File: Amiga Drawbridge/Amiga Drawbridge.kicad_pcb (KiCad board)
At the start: 2 copper layers, 90 x 94 mm, 19 parts, among them J1 FDC, J2 PWR_EXT1, J3 PWR_DRV, J4 PWR_EXT2, M1 Mounting, M2 Mounting, M3 Mounting, M4 Mounting

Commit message: Changed power pin order
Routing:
- net Net-(D1-Pad2): track 126.8 -> 128.6 mm
- net Net-(J3-Pad4): track 15.0 -> 16.6 mm
- net GND: track 0.00 -> 1.27 mm

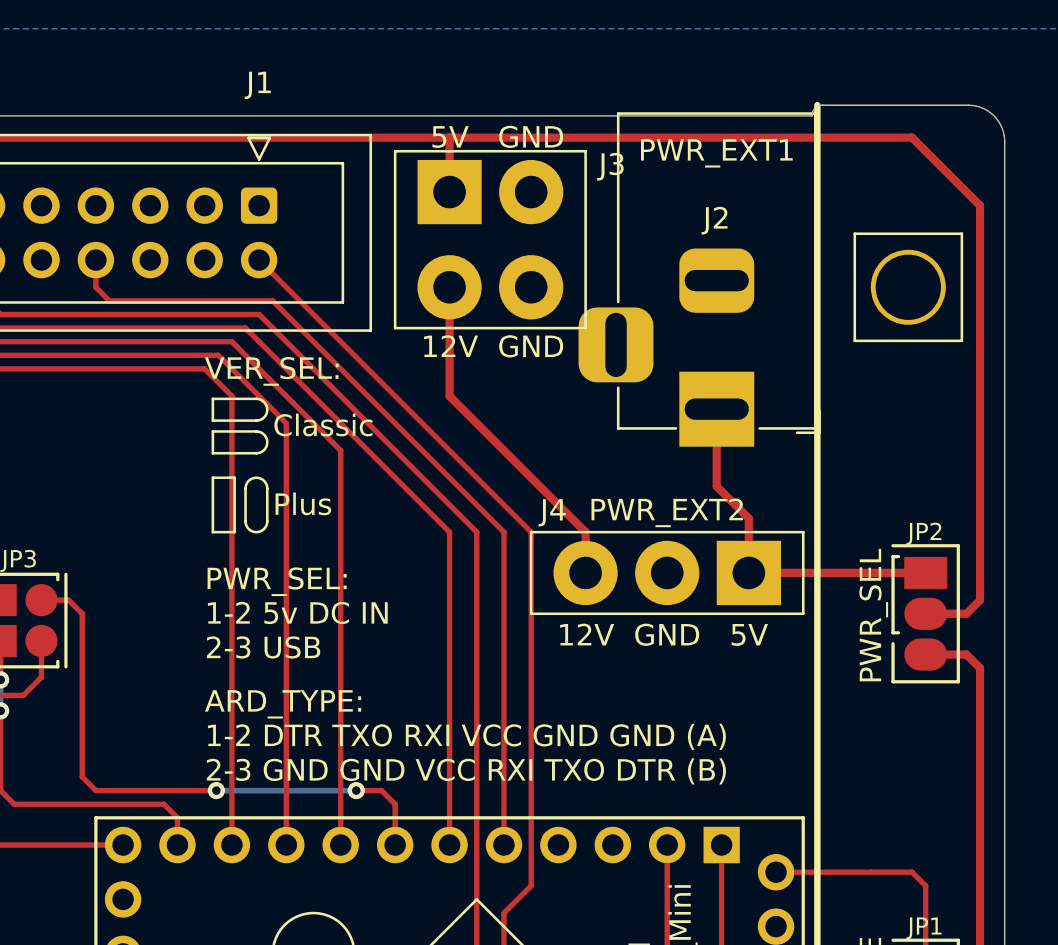
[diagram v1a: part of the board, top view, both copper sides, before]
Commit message: PWR_EXT2 renamed PWR_IN2, now 4 pin to match greaseweazle
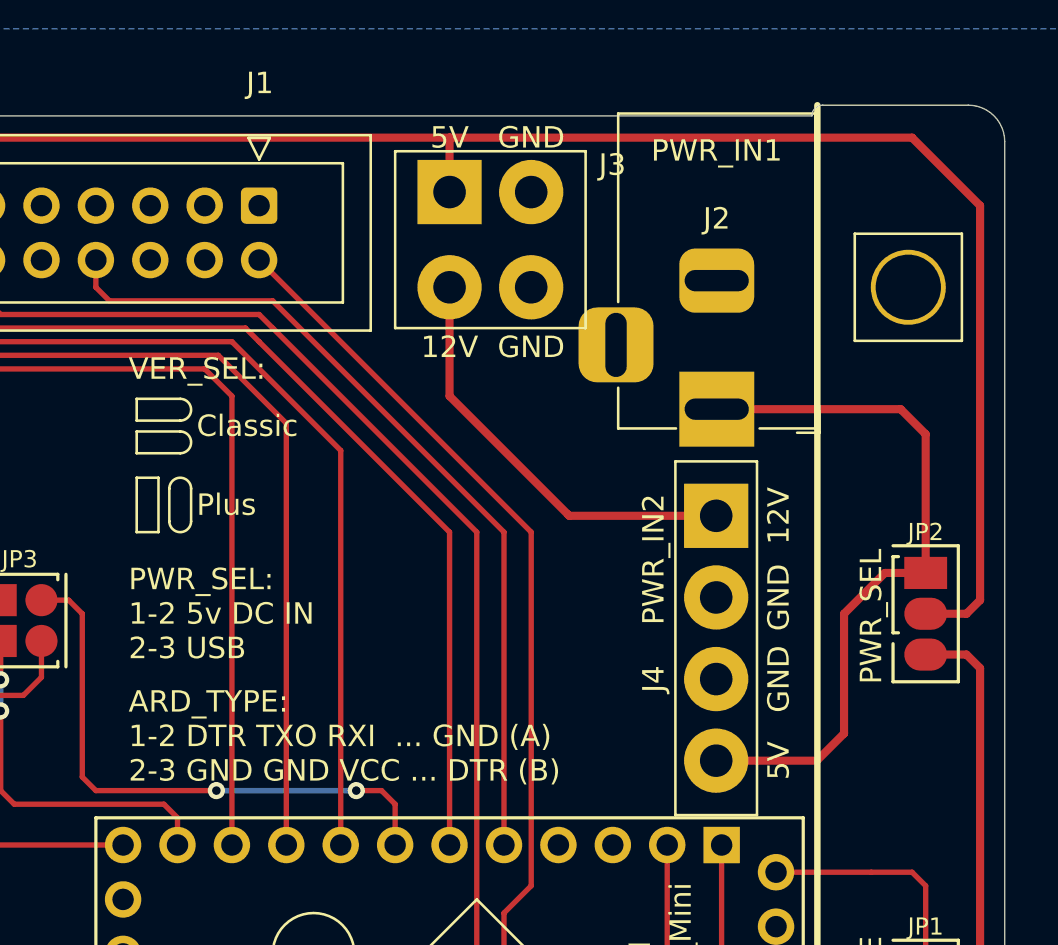
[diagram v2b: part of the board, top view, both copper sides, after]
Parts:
- J2: value PWR_EXT1 -> PWR_IN1
- J4: value PWR_EXT2 -> PWR_IN2; footprint pwr_drv:PWR_EXT -> pwr_drv:PWR_IN
- moved J4 5.83 mm to (187.7, 78.0), turned to 90 degrees
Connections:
- J4 pad 1: Net-(J2-Pad1) -> Net-(J3-Pad4)
- J4 pad 3: Net-(J3-Pad4) -> GND
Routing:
- net Net-(J2-Pad1): track 25.7 -> 33.4 mm
- net Net-(J3-Pad4): track 16.6 -> 19.8 mm
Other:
- board text added: "ARD_TYPE: 1-2 DTR TXO RXI ... GND (A) 2-3 GND GND VCC ... DTR (B)"
- board text removed: "ARD_TYPE: 1-2 DTR TXO RXI VCC GND GND (A) 2-3 GND GND VCC RXI TXO DTR (B)"
